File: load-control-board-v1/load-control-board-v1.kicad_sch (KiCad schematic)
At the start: 37 parts, among them U1 LM317_SOT-223, U2 74AHC1G04, U22 TL081HIDR, U3 LM317_SOT-223, U5 REF5025AD, U6 SN74LVC1G123DCUR_C352969, U7 TL081HIDR, U8 OPA188xxDBV, U9 PZ127-2-10-S

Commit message: Move to layout stage
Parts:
- TP1: footprint TestPoint:TestPoint_Keystone_5019_Miniature -> TestPoint:TestPoint_Keystone_5015_Micro_Mini
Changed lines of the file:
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@@
 			)
 		)
-		(property "Footprint" "TestPoint:TestPoint_Keystone_5019_Miniature"
+		(property "Footprint" "TestPoint:TestPoint_Keystone_5015_Micro_Mini"
 			(at 45.72 152.4 0)
 			(effects

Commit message: initial layout
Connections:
- net +5V: now also C3.1, R2.1, U1.2 (VO)
- net 5V: no longer C3.1, R2.1, U1.2 (VO)
- no-connect marks 5 -> 8
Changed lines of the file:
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@@
 	)
 	(no_connect
+		(at 186.69 81.28)
+	)
+	(no_connect
+		(at 186.69 73.66)
+	)
+	(no_connect
 		(at 276.86 166.37)
 	)
 	(no_connect
+		(at 186.69 76.2)
+	)
+	(no_connect
 		(at 276.86 168.91)
 	)
@@
 	)
 	(global_label "READY"
-		(shape input)
+		(shape output)
 		(at 323.85 105.41 0)
 		(fields_autoplaced yes)
@@
 	)
 	(symbol
+		(lib_id "power:+5V")
+		(at 83.82 153.67 0)
+		(unit 1)
+		(exclude_from_sim no)
+		(in_bom yes)
+		(on_board yes)
+		(dnp no)
+		(fields_autoplaced yes)
+		(property "Reference" "#PWR08"
+			(at 83.82 157.48 0)
+			(effects
+				(font
+					(size 1.27 1.27)
+				)
+				(hide yes)
+			)
+		)
+		(property "Value" "+5V"
+			(at 83.82 148.59 0)
+			(effects
+				(font
+					(size 1.27 1.27)
+				)
+			)
+		)
+		(property "Footprint" ""
+			(at 83.82 153.67 0)
+			(effects
+				(font
+					(size 1.27 1.27)
+				)
+				(hide yes)
+			)
+		)
+		(property "Datasheet" ""
+			(at 83.82 153.67 0)
+			(effects
+				(font
+					(size 1.27 1.27)
+				)
+				(hide yes)
+			)
+		)
+		(property "Description" "Power symbol creates a global label with name \"+5V\""
+			(at 83.82 153.67 0)
+			(effects
+				(font
+					(size 1.27 1.27)
+				)
+				(hide yes)
+			)
+		)
+		(pin "1"
+		)
+		(instances
+			(project ""
+				(path "/932aba27-7b64-4a5e-ae3c-58efe17592af"
+					(reference "#PWR08")
+					(unit 1)
+				)
+			)
+		)
+	)
+	(symbol
 		(lib_id "power:GNDPWR")
 		(at 91.44 185.42 0)
@@
 	)
 	(symbol
-		(lib_id "power:VBUS")
-		(at 83.82 153.67 0)
-		(unit 1)
-		(exclude_from_sim no)
-		(in_bom yes)
-		(on_board yes)
-		(dnp no)
-		(property "Reference" "#PWR08"
-			(at 83.82 157.48 0)
-			(effects
-				(font
-					(size 1.27 1.27)
-				)
-				(hide yes)
-			)
-		)
-		(property "Value" "5V"
-			(at 84.074 149.606 0)
-			(effects
-				(font
-					(size 1.27 1.27)
-				)
-				(justify left)
-			)
-		)
-		(property "Footprint" ""
-			(at 83.82 153.67 0)
-			(effects
-				(font
-					(size 1.27 1.27)
-				)
-				(hide yes)
-			)
-		)
-		(property "Datasheet" ""
-			(at 83.82 153.67 0)
-			(effects
-				(font
-					(size 1.27 1.27)
-				)
-				(hide yes)
-			)
-		)
-		(property "Description" "Power symbol creates a global label with name \"VBUS\""
-			(at 83.82 153.67 0)
-			(effects
-				(font
-					(size 1.27 1.27)
-				)
-				(hide yes)
-			)
-		)
-		(pin "1"
-		)
-		(instances
-			(project "load-control-board-v1"
-				(path "/932aba27-7b64-4a5e-ae3c-58efe17592af"
-					(reference "#PWR08")
-					(unit 1)
-				)
-			)
-		)
-	)
-	(symbol
 		(lib_id "Device:R")
 		(at 128.27 57.15 0)
@@
 		(size 40.894 26.035)
 		(exclude_from_sim no)
-		(in_bom yes)
-		(on_board yes)
-		(dnp no)
+		(in_bom no)
+		(on_board no)
+		(dnp yes)
 		(fields_autoplaced yes)
 		(stroke
@@
 		(size 40.894 26.035)
 		(exclude_from_sim no)
-		(in_bom yes)
-		(on_board yes)
-		(dnp no)
+		(in_bom no)
+		(on_board no)
+		(dnp yes)
 		(fields_autoplaced yes)
 		(stroke
@@
 		(size 40.894 26.035)
 		(exclude_from_sim no)
-		(in_bom yes)
-		(on_board yes)
-		(dnp no)
+		(in_bom no)
+		(on_board no)
+		(dnp yes)
 		(fields_autoplaced yes)
 		(stroke

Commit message: Add connector
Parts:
- added TP10: +5v, TestPoint:TestPoint_Keystone_5015_Micro_Mini, symbol Connector:TestPoint
- added TP11: +12v, TestPoint:TestPoint_Keystone_5015_Micro_Mini, symbol Connector:TestPoint
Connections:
- net +5V: now also TP10.1
- net +9V: now also TP11.1
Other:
- note added: "low temperature coefficient resistor required"
- moved on the sheet: C10, C5, C7, C9, R10, R13, R4, R5, R8, R9, U6, U7

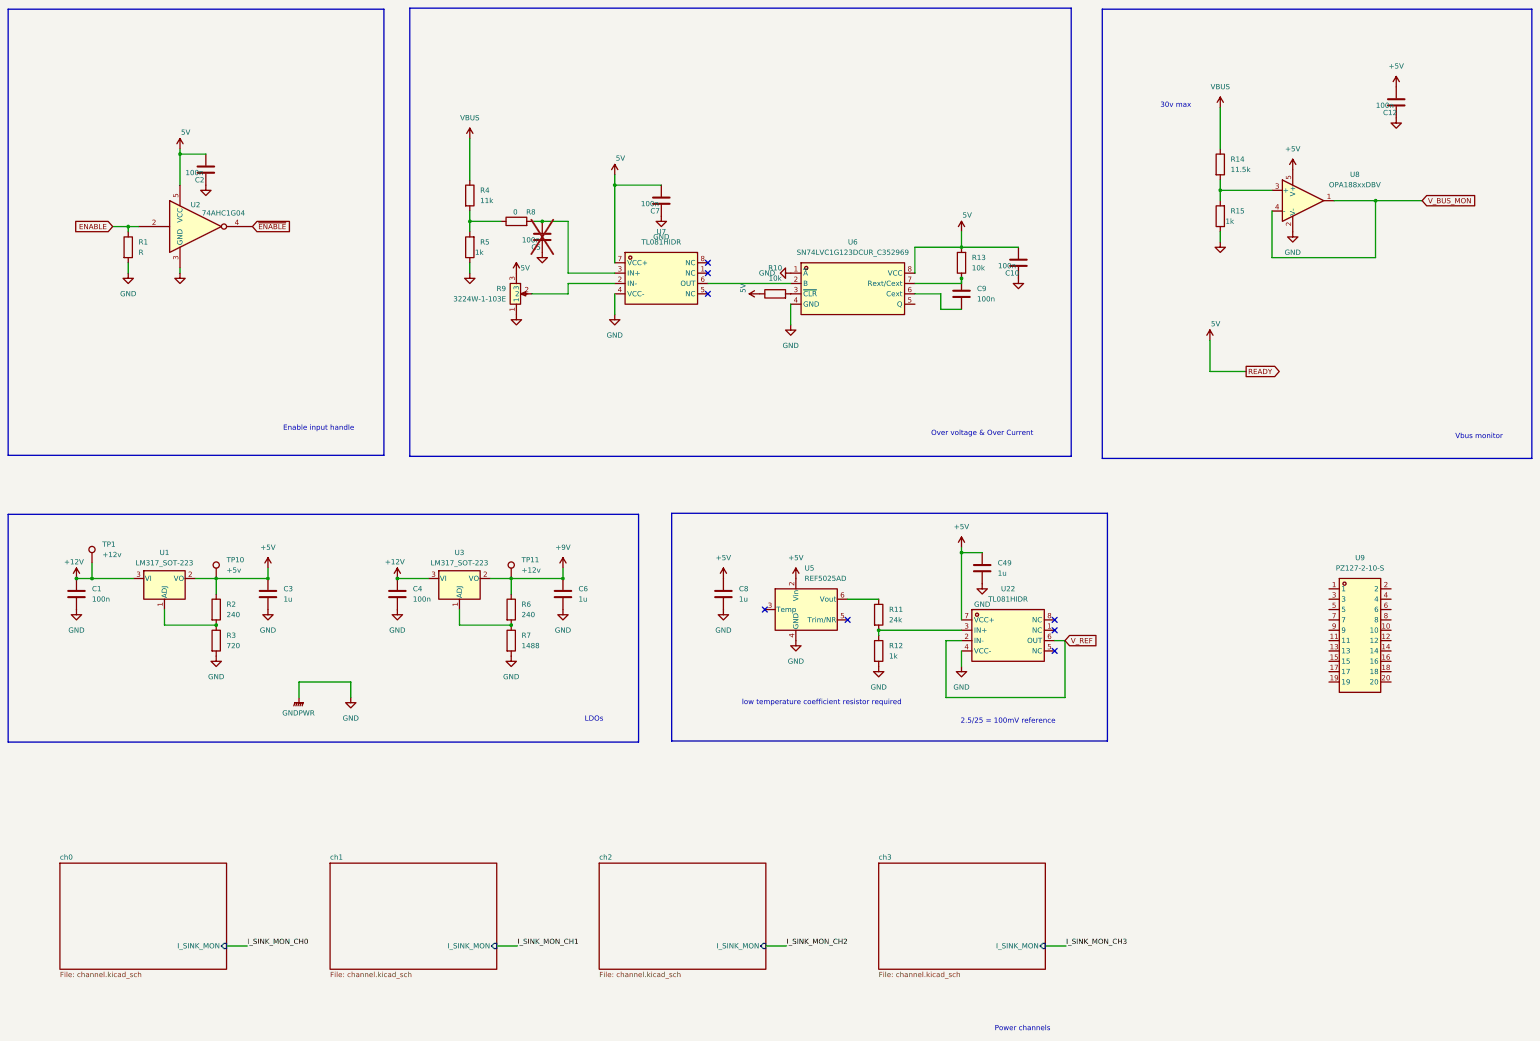
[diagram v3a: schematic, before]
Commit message: Define the connector pinout to control board, import current connector
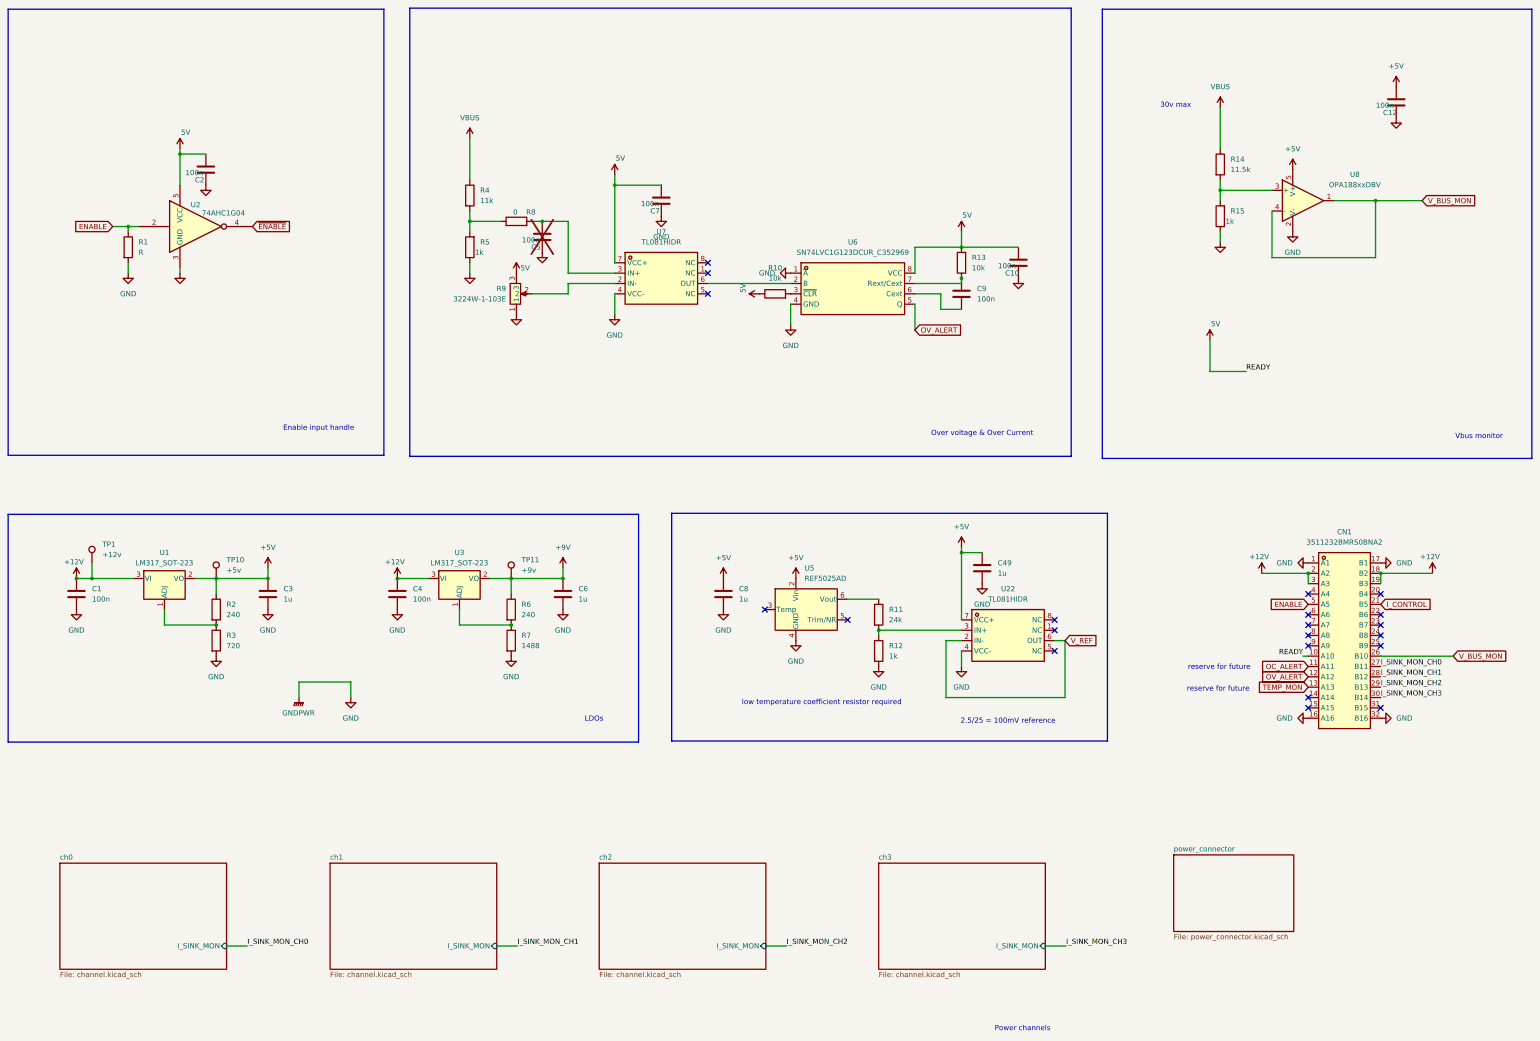
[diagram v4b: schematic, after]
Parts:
- removed U9: PZ127-2-10-S, programmable-load-library:HDR-SMD_PZ127-2-10-S, symbol programmable-load-library:PZ127-2-10-S
- added CN1: 3511232BMRS0BNA2, programmable-load-library:CONN-TH_3511232BMRS0BNA2, symbol programmable-load-library:3511232BMRS0BNA2
- TP11: value +12v -> +9v
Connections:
- net +12V: now also CN1.18 (B2), CN1.19 (B3), CN1.2 (A2), CN1.3 (A3)
- net 5V: now also CN1.10 (A10)
- net ENABLE: now also CN1.5 (A5)
- net GND: now also CN1.1 (A1), CN1.16 (A16), CN1.17 (B1), CN1.32 (B16)
- net I_SINK_MON_CH0: now also CN1.27 (B11)
- net I_SINK_MON_CH1: now also CN1.28 (B12)
- net I_SINK_MON_CH2: now also CN1.29 (B13)
- net I_SINK_MON_CH3: now also CN1.30 (B14)
- net V_BUS_MON: now also CN1.26 (B10)
- net OV_ALERT: now reaches U6.5 (Q)
- net OV_ALERT: now also CN1.12 (A12)
- new net I_CONTROL: CN1.21 (B5)
- new net OC_ALERT: CN1.11 (A11)
- new net TEMP_MON: CN1.13 (A13)
- no-connect marks 8 -> 21
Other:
- added sheet power_connector (power_connector.kicad_sch)
- note added: "reserve for future"

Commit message: layout before check
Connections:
- net +5V: now also C10.2, C2.2, C7.2, CN1.10 (A10), R13.2, U2.5 (VCC), U6.8 (VCC), U7.7 (VCC+)
- net 5V: no longer C10.2, C2.2, C7.2, CN1.10 (A10), R13.2, U2.5 (VCC), U6.8 (VCC), U7.7 (VCC+)
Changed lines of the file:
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@@
 			)
 		)
-		(property "Value" "5V"
+		(property "Value" "+5V"
 			(at 254.254 67.056 0)
 			(effects
@@
 			)
 		)
-		(property "Value" "5V"
+		(property "Value" "+5V"
 			(at 315.214 93.726 0)
 			(effects
@@
 			)
 		)
-		(property "Value" "5V"
+		(property "Value" "+5V"
 			(at 62.484 46.736 0)
 			(effects
@@
 			)
 		)
-		(property "Value" "5V"
+		(property "Value" "+5V"
 			(at 169.164 53.086 0)
 			(effects
